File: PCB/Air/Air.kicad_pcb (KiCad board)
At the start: 2 copper layers, 60 x 110 mm, 15 parts, among them J1 Conn_01x02_Socket, M1 Fan, M2 Fan, M3 Fan, Q1 NMOS, Q2 NMOS, Q3 NMOS, U1 LM7805_TO220, U2 WRL-00691

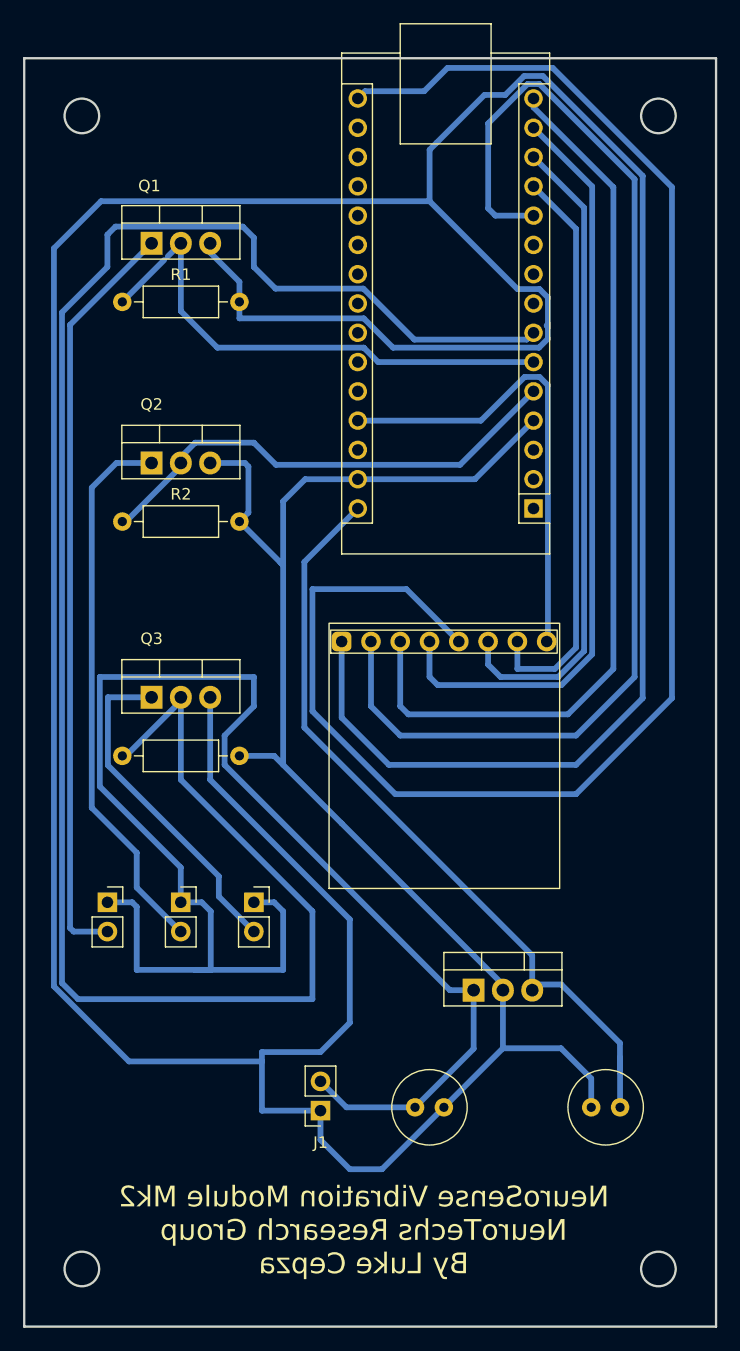
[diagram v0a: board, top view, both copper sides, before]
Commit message: Updated PCB files; added desing files for caress and vibration
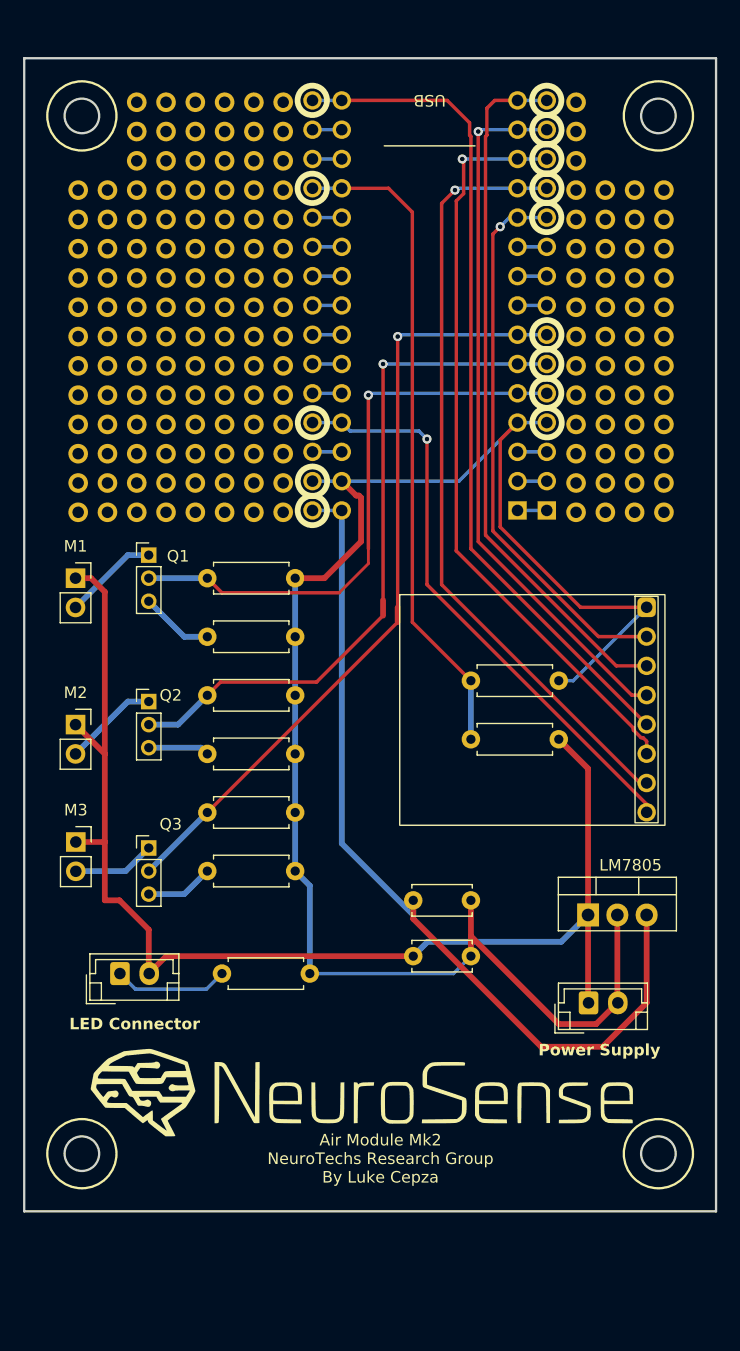
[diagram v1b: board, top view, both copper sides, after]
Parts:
- removed U1: LM7805_TO220, Package_TO_SOT_THT:TO-220-3_Vertical
- added G***: LOGO, Logo:NeuroSenseLogo50mm, F.Cu at (69.6, 129.4)
- added J2: Battery, Connector_JST:JST_EH_B2B-EH-A_1x02_P2.50mm_Vertical, F.Cu at (88.9, 121.9)
- added LM7805: LM7805_TO220, Package_TO_SOT_THT:TO-220-3_Vertical, F.Cu at (88.9, 114.3)
- added R4: 80k, Resistor_THT:R_Axial_DIN0207_L6.3mm_D2.5mm_P7.62mm_Horizontal, F.Cu at (86.4, 99.1)
- added R5: 50K, Resistor_THT:R_Axial_DIN0207_L6.3mm_D2.5mm_P7.62mm_Horizontal, F.Cu at (78.7, 94.0)
- added R6: 3.3k, Resistor_THT:R_Axial_DIN0207_L6.3mm_D2.5mm_P7.62mm_Horizontal, F.Cu at (57.1, 119.4)
- added R7: 100, Resistor_THT:R_Axial_DIN0207_L6.3mm_D2.5mm_P7.62mm_Horizontal, F.Cu at (55.9, 100.3)
- added R8: 3.3 k, Resistor_THT:R_Axial_DIN0207_L6.3mm_D2.5mm_P7.62mm_Horizontal, F.Cu at (55.9, 105.4)
- added R9: 100, Resistor_THT:R_Axial_DIN0207_L6.3mm_D2.5mm_P7.62mm_Horizontal, F.Cu at (55.9, 110.5)
- added REF**: PinHeader_1x15_P2.54mm_Vertical, Mods:PinHeader_1x15_P2.54mm_Vertical, F.Cu at (52.3, 43.8)
- added REF**: PinHeader_1x12_moded, Mods:PinHeader_1x12_moded, F.Cu at (90.4, 51.4)
- added REF**: PinHeader_1x15_P2.54mm_Vertical, Mods:PinHeader_1x15_P2.54mm_Vertical, F.Cu at (59.9, 43.8)
- added REF**: PinHeader_1x15_P2.54mm_Vertical, Mods:PinHeader_1x15_P2.54mm_Vertical, F.Cu at (49.8, 43.8)
- added REF**: PinHeader_1x15_P2.54mm_Vertical, Mods:PinHeader_1x15_P2.54mm_Vertical, F.Cu at (87.9, 43.8)
- added REF**: PinHeader_1x12_moded, Mods:PinHeader_1x12_moded, F.Cu at (95.5, 51.4)
- added REF**: PinHeader_1x12_moded, Mods:PinHeader_1x12_moded, F.Cu at (92.9, 51.4)
- added REF**: PinHeader_1x15_P2.54mm_Vertical, Mods:PinHeader_1x15_P2.54mm_Vertical, F.Cu at (54.8, 43.8)
- added REF**: PinHeader_1x15_P2.54mm_Vertical, Mods:PinHeader_1x15_P2.54mm_Vertical, F.Cu at (62.5, 43.8)
- added REF**: PinHeader_1x12_moded, Mods:PinHeader_1x12_moded, F.Cu at (44.7, 51.4)
- added REF**: PinHeader_1x12_moded, Mods:PinHeader_1x12_moded, F.Cu at (47.2, 51.4)
- added REF**: PinHeader_1x15_P2.54mm_Vertical, Mods:PinHeader_1x15_P2.54mm_Vertical, F.Cu at (57.4, 43.8)
- A1: footprint Module:Arduino_Nano -> Mods:Arduino_Nano_Connectors side by
- C1: value 220 uF -> 33uF; footprint Capacitor_THT:C_Radial_D6.3mm_H5.0mm_P2.50mm -> Capacitor_THT:C_Disc_D5.0mm_W2.5mm_P5.00mm
- C2: footprint Capacitor_THT:C_Radial_D6.3mm_H5.0mm_P2.50mm -> Capacitor_THT:C_Disc_D5.0mm_W2.5mm_P5.00mm
- J1: value Conn_01x02_Socket -> LED; footprint Connector_PinSocket_2.54mm:PinSocket_1x02_P2.54mm_Vertical -> Connector_JST:JST_EH_B2B-EH-A_1x02_P2.50mm_Vertical
- Q1, Q2, Q3: value NMOS -> NPN; footprint Package_TO_SOT_THT:TO-220-3_Vertical -> Connector_PinHeader_2.00mm:PinHeader_1x03_P2.00mm_Vertical
- R1: footprint Resistor_THT:R_Axial_DIN0207_L6.3mm_D2.5mm_P10.16mm_Horizontal -> Resistor_THT:R_Axial_DIN0207_L6.3mm_D2.5mm_P7.62mm_Horizontal
- R2: value 3.3 k -> 100; footprint Resistor_THT:R_Axial_DIN0207_L6.3mm_D2.5mm_P10.16mm_Horizontal -> Resistor_THT:R_Axial_DIN0207_L6.3mm_D2.5mm_P7.62mm_Horizontal
- R3: value 3.3 k -> 3.3 k; footprint Resistor_THT:R_Axial_DIN0207_L6.3mm_D2.5mm_P10.16mm_Horizontal -> Resistor_THT:R_Axial_DIN0207_L6.3mm_D2.5mm_P7.62mm_Horizontal
- moved M1 28.2 mm to (44.5, 85.1)
- moved Q1 27.0 mm to (50.8, 83.1)
- moved C2 25.4 mm to (73.7, 113.0), turned to 0 degrees
- moved R1 25.1 mm to (55.9, 85.1)
- moved U2 21.6 mm to (85.7, 87.5), turned to 0 degrees
- moved J1 21.1 mm to (48.3, 119.4), turned to 0 degrees
- moved Q2 20.7 mm to (50.8, 95.8)
- moved M2 17.9 mm to (44.5, 97.8)
- moved M3 16.3 mm to (44.5, 108.0)
- moved C1 13.1 mm to (73.7, 117.9)
- moved Q3 13.1 mm to (50.8, 108.5)
- moved R2 12.4 mm to (55.9, 90.2)
- moved R3 9.05 mm to (55.9, 95.2)
- moved A1 1.40 mm to (82.8, 79.2)
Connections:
- net Net-(A1-D10) renamed /D10_CSN
- net Net-(A1-D11) renamed /D11_MOSI
- net Net-(A1-D12) renamed /D12_MISO
- net Net-(A1-D13) renamed /D13_SCK
- net Net-(A1-D8) renamed /D8_IRQ
- net Net-(A1-D9) renamed /D9_CE
- net Net-(A1-VIN) renamed /VIN_5v
- A1 pad 19: unconnected-(A1-A0-Pad19) -> /A0_VBat
- A1 pad 5: Net-(A1-D2) -> /D2_F1
- A1 pad 6: Net-(A1-D3) -> /D3_F2
- A1 pad 7: Net-(A1-D4) -> /D4_F3
- J1 pad 1: GND -> Net-(J1-Pin_1)
- Q1 pad 2: Net-(A1-D3) -> /D2_F1
- Q1 pad 3: GND -> Net-(Q1-E)
- Q2 pad 2: Net-(A1-D2) -> /D3_F2
- Q2 pad 3: GND -> Net-(Q2-E)
- Q3 pad 2: Net-(A1-D4) -> /D4_F3
- Q3 pad 3: GND -> Net-(Q3-E)
- R1 pad 1: Net-(A1-D3) -> /D2_F1
- R2 pad 1: Net-(A1-D2) -> Net-(Q1-E)
- R3 pad 1: Net-(A1-D4) -> /D3_F2
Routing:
- net GND: track 468.7 -> 149.5 mm
- net Net-(A1-D4): track 170.1 -> 0.00 mm
- net /D4_F3: track 0.00 -> 68.3 mm, vias 0 -> 1
- net /D13_SCK: track 139.7 -> 73.0 mm
- net /D3_F2: track 0.00 -> 60.3 mm, vias 0 -> 1
- net Net-(M1--): track 66.4 -> 8.23 mm
- net /A0_VBat: track 0.00 -> 57.3 mm
- net /D8_IRQ: track 103.9 -> 48.1 mm, vias 0 -> 1
- net /D2_F1: track 0.00 -> 50.8 mm, vias 0 -> 1
- net Net-(A1-D3): track 45.0 -> 0.00 mm
- net Net-(A1-D2): track 42.4 -> 0.00 mm
- net Net-(M2--): track 47.8 -> 8.23 mm
- net +12V: track 133.9 -> 108.7 mm
- net Net-(M3--): track 29.4 -> 7.16 mm
- net /D9_CE: track 49.8 -> 67.6 mm, vias 0 -> 1
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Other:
- board size 60 x 110 mm -> 60 x 100 mm
- board text added: "Air Module Mk2 NeuroTechs Research Group By Luke Cepza"
- board text added: "LED Connector"
- board text added: "Power Supply"
- board text removed: "NeuroSense Vibration Module Mk2 NeuroTechs Research Group By Luke Cepza"
